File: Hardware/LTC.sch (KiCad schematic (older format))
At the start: 82 parts, among them J10 Conn_01x01_Female, J11 Conn_01x01_Female, J12 Conn_01x01_Female, J6 Conn_01x01_Female, J7 Conn_01x01_Female, J8 Conn_01x01_Female, J9 Conn_01x01_Female, Q2 Q_PMOS_GSD, Q3 Q_PMOS_GSD, Q4 Q_PMOS_GSD, Q5 Q_PMOS_GSD, Q6 Q_PMOS_GSD, Q7 Q_PMOS_GSD, Q8 Q_PMOS_GSD, Q9 Q_NPN_BCE

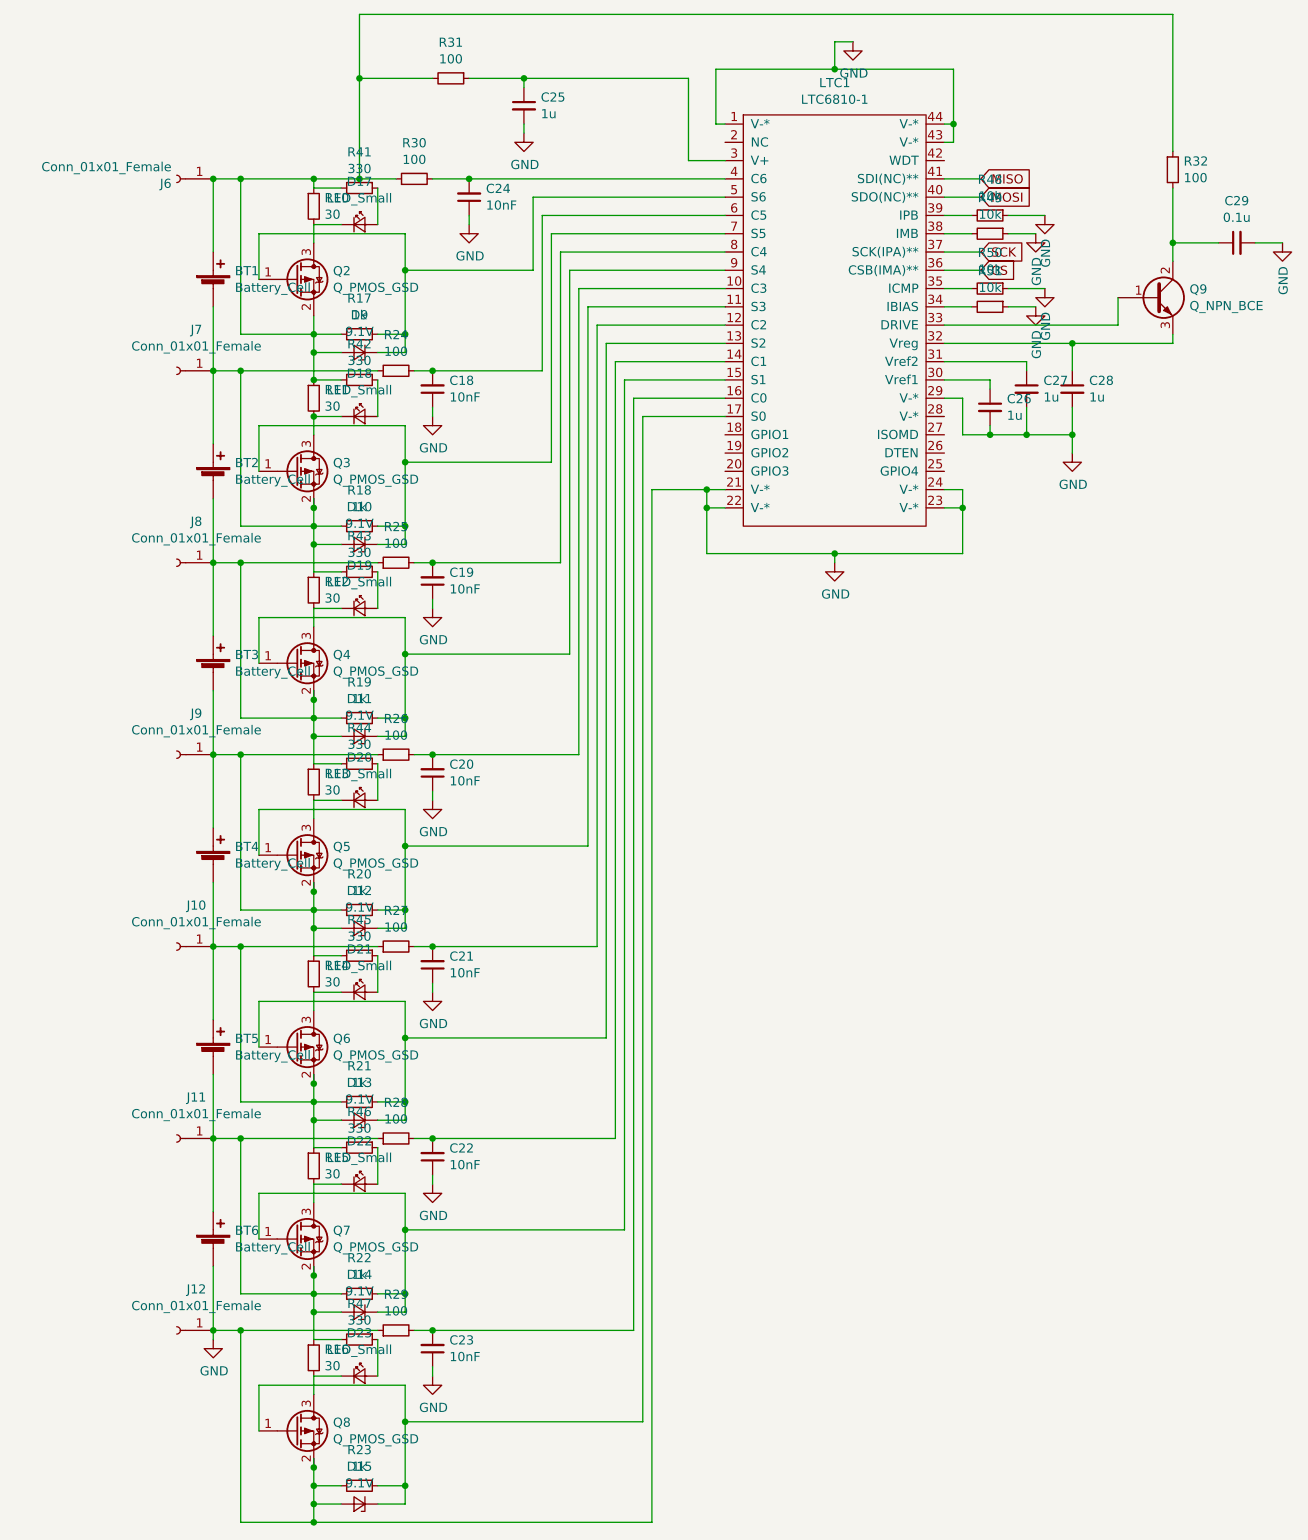
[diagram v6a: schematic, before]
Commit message: PCB v2
changes in scheme:
NMOS->PMOS in LTC balance
S6 LTC pinout deleted
another discharge resistor added on every S# LTC pinout and value changed from 30 to 68 on both
PCB changes:
CAN position changed
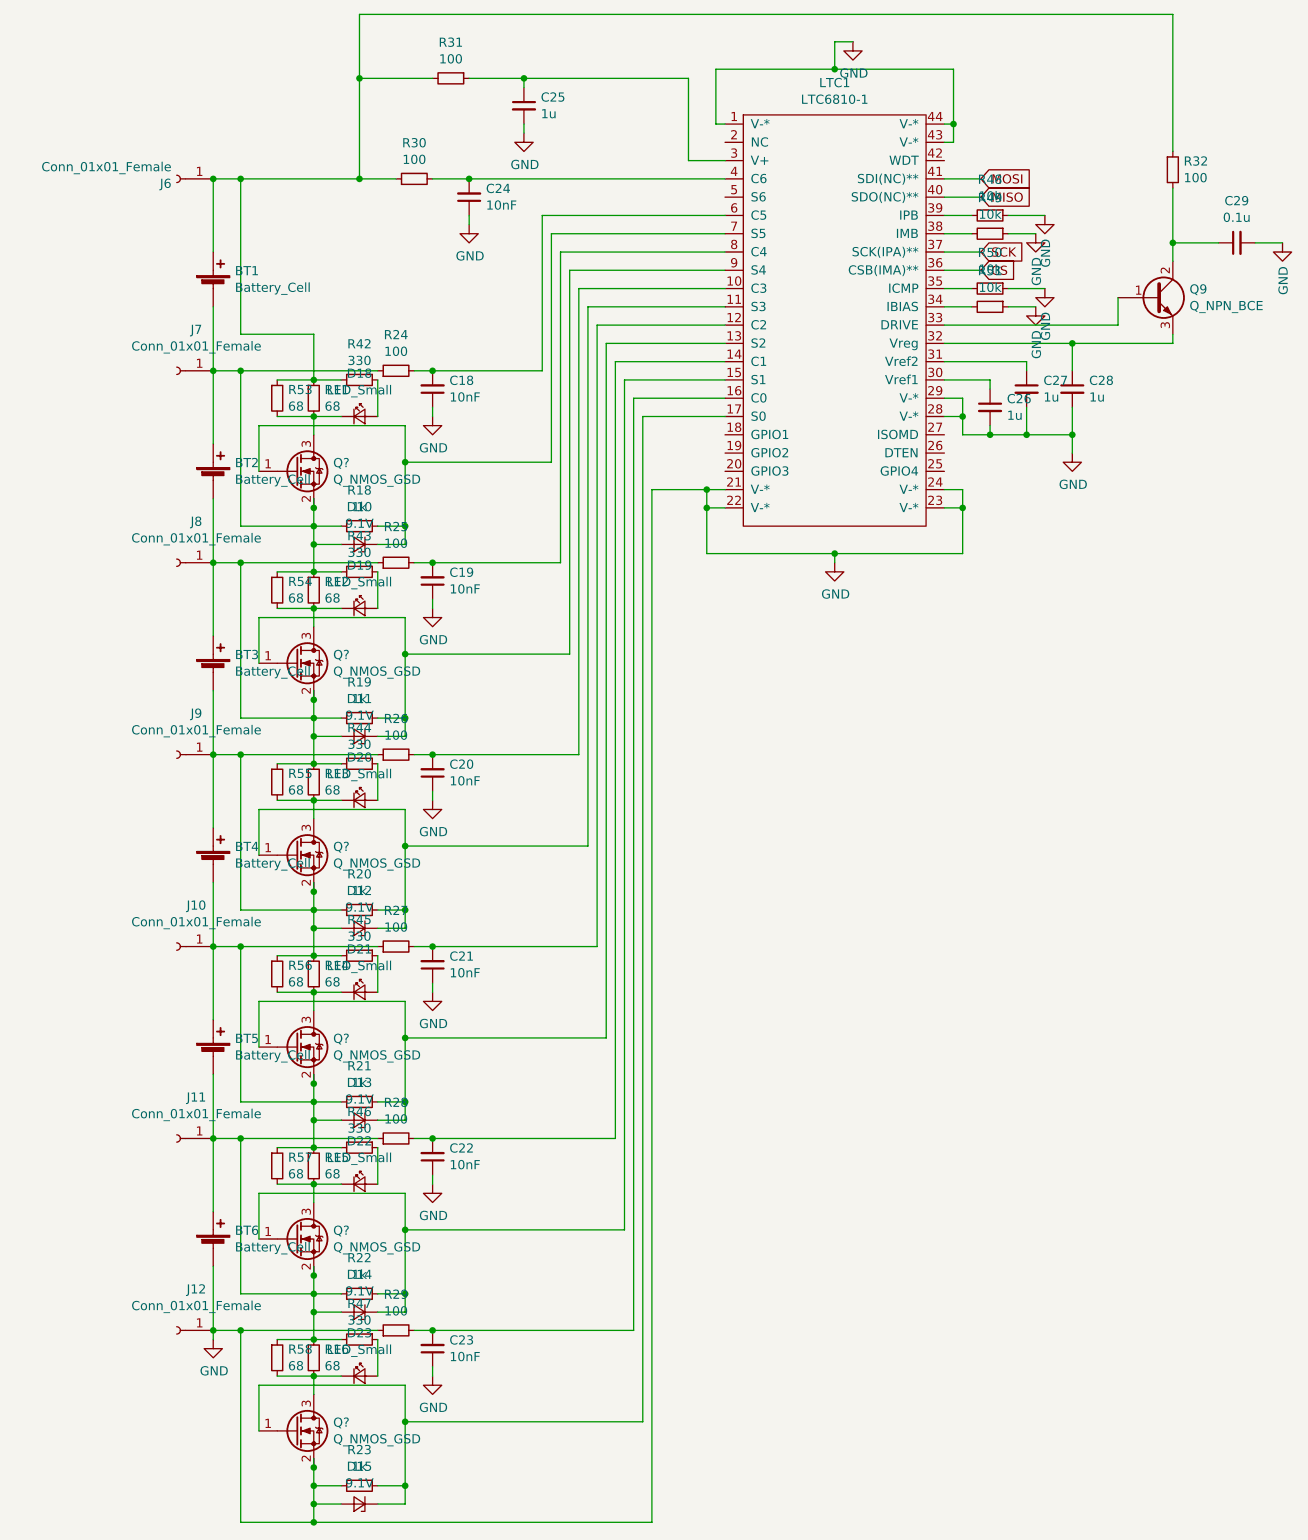
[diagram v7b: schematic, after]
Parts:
- removed D17: LED_Small, LED_SMD:LED_0805_2012Metric, symbol Device:LED_Small
- removed D9: 9.1V, Diode_SMD:D_SMB, symbol Device:D_Zener_Small
- removed Q2, Q3, Q4, Q5, Q6, Q7, Q8: Q_PMOS_GSD, Package_TO_SOT_SMD:SOT-23W, symbol Device:Q_PMOS_GSD
- removed R10: 30, Resistor_SMD:R_2512_6332Metric, symbol Device:R_Small
- removed R17: 1k, Resistor_SMD:R_1206_3216Metric, symbol Device:R_Small
- removed R41: 330, Resistor_SMD:R_1206_3216Metric, symbol Device:R_Small
- added Q? (x6): Q_NMOS_GSD, symbol Device:Q_NMOS_GSD
- added R53, R54, R55, R56, R57, R58: 68, Resistor_SMD:R_2512_6332Metric, symbol Device:R_Small
- R11, R12, R13, R14, R15, R16: value 30 -> 68
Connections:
- net GND: now also LTC1.28 (V-*), Q?.2 (S)
- net MISO: now also LTC1.40 (SDO(NC)**); no longer LTC1.41 (SDI(NC)**)
- net MOSI: now also LTC1.41 (SDI(NC)**); no longer LTC1.40 (SDO(NC)**)
- net at D12.1 (K), LTC1.11 (S3), R20.1: now also Q?.1 (G)
- net at D13.1 (K), LTC1.13 (S2), R21.1: now also Q?.1 (G)
- net at D14.1 (K), LTC1.15 (S1), R22.1: now also Q?.1 (G)
- net at D15.1 (K), LTC1.17 (S0), R23.1: now also Q?.1 (G)
- net at D10.1 (K), LTC1.7 (S5), R18.1: now also Q?.1 (G)
- net at D11.1 (K), LTC1.9 (S4), R19.1: now also Q?.1 (G)
- net at BT1.1 (+), J6.1 (Pin_1), R11.1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: now also R53.1
- net at BT1.2 (-), BT2.1 (+), D10.2 (A)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: now also Q?.2 (S), R54.1
- net at D18.1 (K), R11.2: now also Q?.3 (D), R53.2
- net at BT2.2 (-), BT3.1 (+), D11.2 (A)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: now also Q?.2 (S), R55.1
- net at BT3.2 (-), BT4.1 (+), D12.2 (A)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: now also Q?.2 (S), R56.1
- net at D19.1 (K), R12.2: now also Q?.3 (D), R54.2
- net at BT4.2 (-), BT5.1 (+), D13.2 (A)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: now also Q?.2 (S), R57.1
- net at D20.1 (K), R13.2: now also Q?.3 (D), R55.2
- net at BT5.2 (-), BT6.1 (+), D14.2 (A)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: now also Q?.2 (S), R58.1
- net at D21.1 (K), R14.2: now also Q?.3 (D), R56.2
- net at D22.1 (K), R15.2: now also Q?.3 (D), R57.2
- net at D23.1 (K), R16.2: now also Q?.3 (D), R58.2

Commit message: PCB finished
PCB finished and ready to check
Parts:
- added J14, J15, J16: Conn_01x02_Male, Connector_PinHeader_2.54mm:PinHeader_1x02_P2.54mm_Vertical, symbol Connector:Conn_01x02_Male
- Q2, Q3, Q4, Q5, Q6, Q7: renamed from Q?; footprint (none) -> Package_TO_SOT_SMD:SOT-23
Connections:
- net at C24.2, LTC1.4 (C6), R30.2: now also J16.2 (Pin_2)
- net at LTC1.5 (S6): now also J14.1 (Pin_1), J15.1 (Pin_1), J16.1 (Pin_1)
- net at C18.2, LTC1.6 (C5), R24.2: now also J15.2 (Pin_2)
- net at D10.1 (K), LTC1.7 (S5), Q2.1 (G)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: now also J14.2 (Pin_2)
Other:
- moved on the sheet: C24
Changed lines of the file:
@@
 EESchema Schematic File Version 4
-LIBS:bmsLV-cache
 EELAYER 30 0
 EELAYER END
@@
 	4100 3800 4900 3800
 Wire Wire Line
-	4900 3800 4900 2550
-Wire Wire Line
-	4850 3300 4850 2450
+	4900 3800 4900 3000
+Wire Wire Line
+	4850 3300 4850 2650
 Wire Wire Line
 	3050 8550 3050 8200
@@
 $EndComp
 Wire Wire Line
-	4450 2450 4450 2500
+	4300 2450 4300 2500
 $Comp
 L Device:Battery_Cell BT2
@@
 	0    -1   -1   0
 $EndComp
-Connection ~ 4450 2250
-Wire Wire Line
-	4250 2250 4450 2250
+Wire Wire Line
+	4250 2250 4300 2250
 $Comp
 L power:GND #PWR042
 U 1 1 5FF957ED
-P 4450 2500
-F 0 "#PWR042" H 4450 2250 50  0001 C CNN
-F 1 "GND" H 4455 2327 50  0000 C CNN
-F 2 "" H 4450 2500 50  0001 C CNN
-F 3 "" H 4450 2500 50  0001 C CNN
-	1    4450 2500
+P 4300 2500
+F 0 "#PWR042" H 4300 2250 50  0001 C CNN
+F 1 "GND" H 4305 2327 50  0000 C CNN
+F 2 "" H 4300 2500 50  0001 C CNN
+F 3 "" H 4300 2500 50  0001 C CNN
+	1    4300 2500
 	1    0    0    -1
 $EndComp
@@
 L Device:C_Small C24
 U 1 1 5FF93E07
-P 4450 2350
-F 0 "C24" H 4358 2304 50  0000 R CNN
-F 1 "10nF" H 4358 2395 50  0000 R CNN
-F 2 "Capacitor_SMD:C_1206_3216Metric" H 4450 2350 50  0001 C CNN
-F 3 "~" H 4450 2350 50  0001 C CNN
-	1    4450 2350
+P 4300 2350
+F 0 "C24" H 4208 2304 50  0000 R CNN
+F 1 "10nF" H 4208 2395 50  0000 R CNN
+F 2 "Capacitor_SMD:C_1206_3216Metric" H 4300 2350 50  0001 C CNN
+F 3 "~" H 4300 2350 50  0001 C CNN
+	1    4300 2350
 	-1   0    0    1
 $EndComp
@@
 Wire Wire Line
 	4850 2450 5850 2450
-Wire Wire Line
-	4450 2250 5850 2250
 Wire Wire Line
 	5450 3950 5750 3950
@@
 	3600 3100 3600 3350
 $Comp
-L Device:Q_NMOS_GSD Q?
+L Device:Q_NMOS_GSD Q2
 U 1 1 60708304
 P 3500 3850
-F 0 "Q?" H 3706 3896 50  0000 L CNN
+F 0 "Q2" H 3706 3896 50  0000 L CNN
 F 1 "Q_NMOS_GSD" H 3706 3805 50  0000 L CNN
-F 2 "" H 3700 3950 50  0001 C CNN
+F 2 "Package_TO_SOT_SMD:SOT-23" H 3700 3950 50  0001 C CNN
 F 3 "~" H 3500 3850 50  0001 C CNN
 	1    3500 3850
@@
 	3600 4050 3600 4150
 $Comp
-L Device:Q_NMOS_GSD Q?
+L Device:Q_NMOS_GSD Q3
 U 1 1 60749739
 P 3500 4900
-F 0 "Q?" H 3706 4946 50  0000 L CNN
+F 0 "Q3" H 3706 4946 50  0000 L CNN
 F 1 "Q_NMOS_GSD" H 3706 4855 50  0000 L CNN
-F 2 "" H 3700 5000 50  0001 C CNN
+F 2 "Package_TO_SOT_SMD:SOT-23" H 3700 5000 50  0001 C CNN
 F 3 "~" H 3500 4900 50  0001 C CNN
 	1    3500 4900
@@
 	3600 6100 3600 6150
 $Comp
-L Device:Q_NMOS_GSD Q?
+L Device:Q_NMOS_GSD Q4
 U 1 1 6078A524
 P 3500 5950
-F 0 "Q?" H 3706 5996 50  0000 L CNN
+F 0 "Q4" H 3706 5996 50  0000 L CNN
 F 1 "Q_NMOS_GSD" H 3706 5905 50  0000 L CNN
-F 2 "" H 3700 6050 50  0001 C CNN
+F 2 "Package_TO_SOT_SMD:SOT-23" H 3700 6050 50  0001 C CNN
 F 3 "~" H 3500 5950 50  0001 C CNN
 	1    3500 5950
@@
 	3600 7150 3600 7200
 $Comp
-L Device:Q_NMOS_GSD Q?
+L Device:Q_NMOS_GSD Q5
 U 1 1 607A07CD
 P 3500 7000
-F 0 "Q?" H 3706 7046 50  0000 L CNN
+F 0 "Q5" H 3706 7046 50  0000 L CNN
 F 1 "Q_NMOS_GSD" H 3706 6955 50  0000 L CNN
-F 2 "" H 3700 7100 50  0001 C CNN
+F 2 "Package_TO_SOT_SMD:SOT-23" H 3700 7100 50  0001 C CNN
 F 3 "~" H 3500 7000 50  0001 C CNN
 	1    3500 7000
@@
 	3600 8200 3600 8250
 $Comp
-L Device:Q_NMOS_GSD Q?
+L Device:Q_NMOS_GSD Q6
 U 1 1 607B6027
 P 3500 8050
-F 0 "Q?" H 3706 8096 50  0000 L CNN
+F 0 "Q6" H 3706 8096 50  0000 L CNN
 F 1 "Q_NMOS_GSD" H 3706 8005 50  0000 L CNN
-F 2 "" H 3700 8150 50  0001 C CNN
+F 2 "Package_TO_SOT_SMD:SOT-23" H 3700 8150 50  0001 C CNN
 F 3 "~" H 3500 8050 50  0001 C CNN
 	1    3500 8050
@@
 	3600 9250 3600 9300
 $Comp
-L Device:Q_NMOS_GSD Q?
+L Device:Q_NMOS_GSD Q7
 U 1 1 607CBEDB
 P 3500 9100
-F 0 "Q?" H 3706 9146 50  0000 L CNN
+F 0 "Q7" H 3706 9146 50  0000 L CNN
 F 1 "Q_NMOS_GSD" H 3706 9055 50  0000 L CNN
-F 2 "" H 3700 9200 50  0001 C CNN
+F 2 "Package_TO_SOT_SMD:SOT-23" H 3700 9200 50  0001 C CNN
 F 3 "~" H 3500 9100 50  0001 C CNN
 	1    3500 9100
@@
 Wire Wire Line
 	7150 3550 7150 3650
+$Comp
+L Connector:Conn_01x02_Male J16
+U 1 1 6042E497
+P 5300 1950
+F 0 "J16" V 5362 1994 50  0000 L CNN
+F 1 "Conn_01x02_Male" V 5453 1994 50  0000 L CNN
+F 2 "Connector_PinHeader_2.54mm:PinHeader_1x02_P2.54mm_Vertical" H 5300 1950 50  0001 C CNN
+F 3 "~" H 5300 1950 50  0001 C CNN
+	1    5300 1950
+	0    1    1    0
+$EndComp
+Wire Wire Line
+	5850 2350 5300 2350
+Wire Wire Line
+	5300 2350 5300 2150
+Wire Wire Line
+	5200 2150 5200 2250
+Connection ~ 5200 2250
+Wire Wire Line
+	5200 2250 5850 2250
+Connection ~ 4300 2250
+Wire Wire Line
+	4300 2250 5200 2250
+$Comp
+L Connector:Conn_01x02_Male J15
+U 1 1 60474109
+P 4500 2550
+F 0 "J15" H 4608 2731 50  0000 C CNN
+F 1 "Conn_01x02_Male" H 4608 2640 50  0000 C CNN
+F 2 "Connector_PinHeader_2.54mm:PinHeader_1x02_P2.54mm_Vertical" H 4500 2550 50  0001 C CNN
+F 3 "~" H 4500 2550 50  0001 C CNN
+	1    4500 2550
+	1    0    0    -1
+$EndComp
+Wire Wire Line
+	5300 2350 4700 2350
+Wire Wire Line
+	4700 2350 4700 2550
+Connection ~ 5300 2350
+Wire Wire Line
+	4700 2650 4850 2650
+Connection ~ 4850 2650
+Wire Wire Line
+	4850 2650 4850 2450
+$Comp
+L Connector:Conn_01x02_Male J14
+U 1 1 604A2535
+P 4250 2900
+F 0 "J14" H 4358 3081 50  0000 C CNN
+F 1 "Conn_01x02_Male" H 4358 2990 50  0000 C CNN
+F 2 "Connector_PinHeader_2.54mm:PinHeader_1x02_P2.54mm_Vertical" H 4250 2900 50  0001 C CNN
+F 3 "~" H 4250 2900 50  0001 C CNN
+	1    4250 2900
+	1    0    0    -1
+$EndComp
+Wire Wire Line
+	4700 2350 4450 2350
+Connection ~ 4700 2350
+Connection ~ 4900 3000
+Wire Wire Line
+	4900 3000 4900 2550
+Wire Wire Line
+	4450 2350 4450 2900
+Wire Wire Line
+	4450 3000 4900 3000
 $EndSCHEMATC
